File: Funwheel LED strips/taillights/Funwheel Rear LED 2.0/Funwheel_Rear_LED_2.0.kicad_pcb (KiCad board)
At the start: 2 copper layers, 6.8 x 155 mm, 36 parts, among them J1 BM04B-GHS-TBT

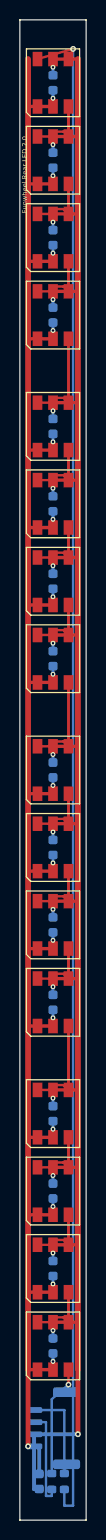
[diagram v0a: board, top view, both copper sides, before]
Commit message: feat: add VFBMS32 AI PCB schematic, layout, and supporting automation scripts
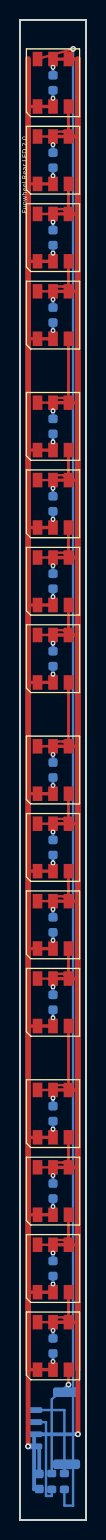
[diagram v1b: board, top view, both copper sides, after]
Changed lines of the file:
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@@
 		(net "DATA_OUT")
+	)
+	(gr_rect
+		(start 0 0)
+		(end 6.85 155)
+		(stroke
+			(width 0.1)
+			(type default)
+		)
+		(fill none)
+		(layer "Edge.Cuts")
 	)
 	(embedded_fonts no)
